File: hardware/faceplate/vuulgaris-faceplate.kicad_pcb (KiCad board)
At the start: 4 copper layers, 298.3 x 137.8 mm, 54 parts, among them J1 HX JN2.54-2x5P TP H8.9, U1 MSP430FR2675TPT, Y1 32.768kHz FC-135 12.5pF

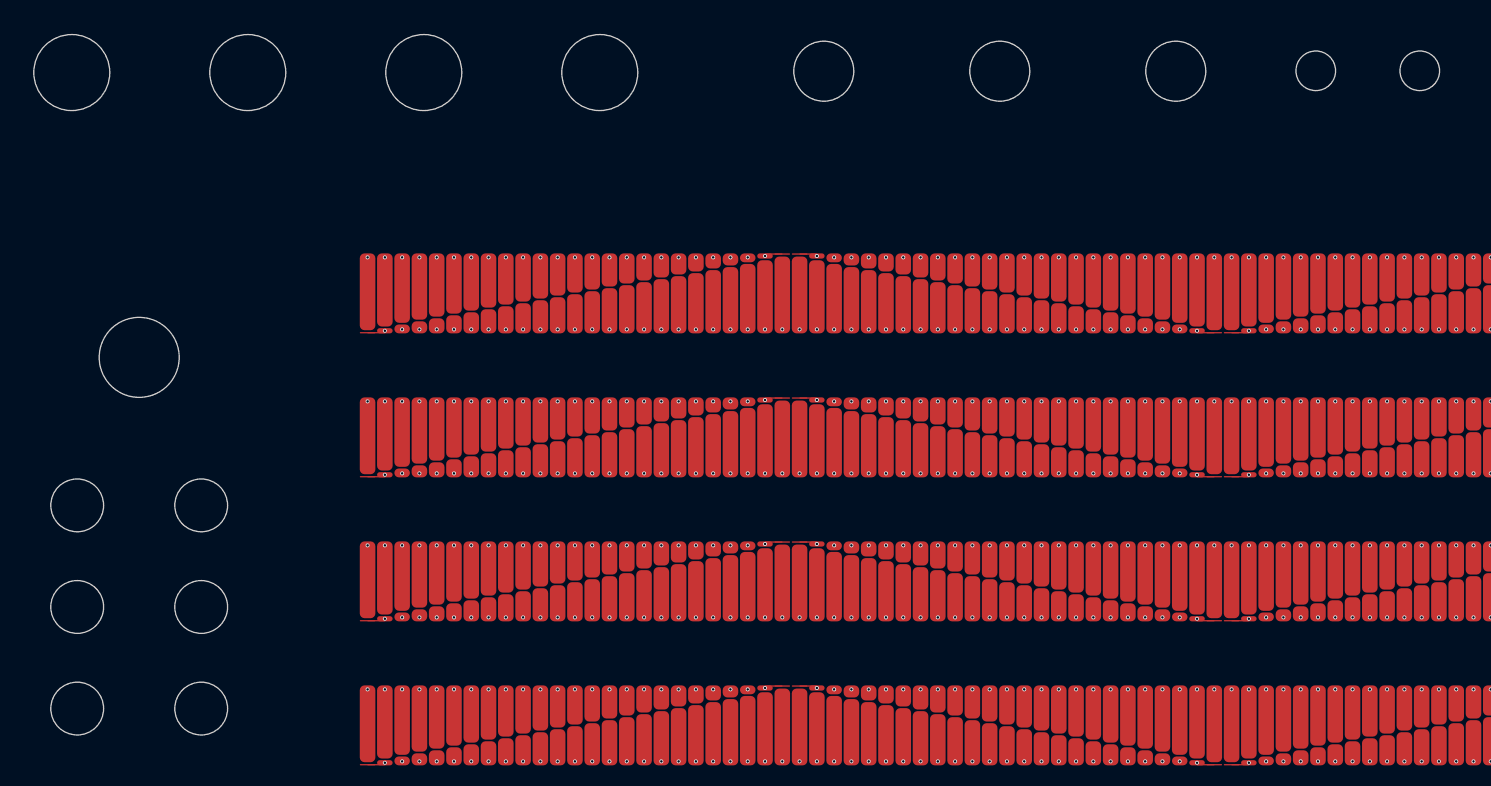
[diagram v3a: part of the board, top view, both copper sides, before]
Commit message: faceplate: bigger button and toggle holes; OLED pixels and glass on F.Fab
Dylan: the button and switch holes look too tight. They were, both by
the drawings:

- Buttons 6.6 -> 7.2. TS1103S: the plunger is 6.2 at our 14mm height and
  one-decimal dimensions are +-0.2, so a 6.4 plunger had 0.1 a side --
  under the faceplate's own +-0.25 float on the pots. A plunger that
  touches its hole is a sticky button. Now 0.4 a side at the largest.
  The generator's mx_hole_r_mm feeds the control-column layout (a bigger
  value re-flows SW4-SW9 on the routed main board -- tried), so it stays
  as the layout value and the new mx_cut_d_mm is what gets routed; the
  physical checks (walls, pads, plunger) use the cut, placement file
  unchanged.
- Toggles 4.95 -> 5.6. Dailywell's bushing is 10-48 UNS, 4.83 over the
  thread; its 4.95 is the hole for a switch hung from the panel by its
  nut. Ours is soldered to the main board too, so the hole takes the
  bushing's +-0.25 and the faceplate's float: 0.39 a side.

New generator rows check both clearances; at the old sizes they fail
(0.10 and 0.06 a side). design-state and the README hole table updated.

Also, as asked: the OLED's active area and glass drawn on the faceplate's
F.Fab from the same numbers as the window (reference only, not
fabricated), so the window reads against the pixels in Pcbnew. mkholes
collects before removing (KiCad 7 bindings again) and is idempotent.

Checked: generator --check all pass, placement unchanged; mksch/netcheck
145/145; boardcheck parity 0, clearance 0; DRC --unrouted 0 errors;
panelcheck --strict 13 OK, 23 holes on their parts; place.py all 24.
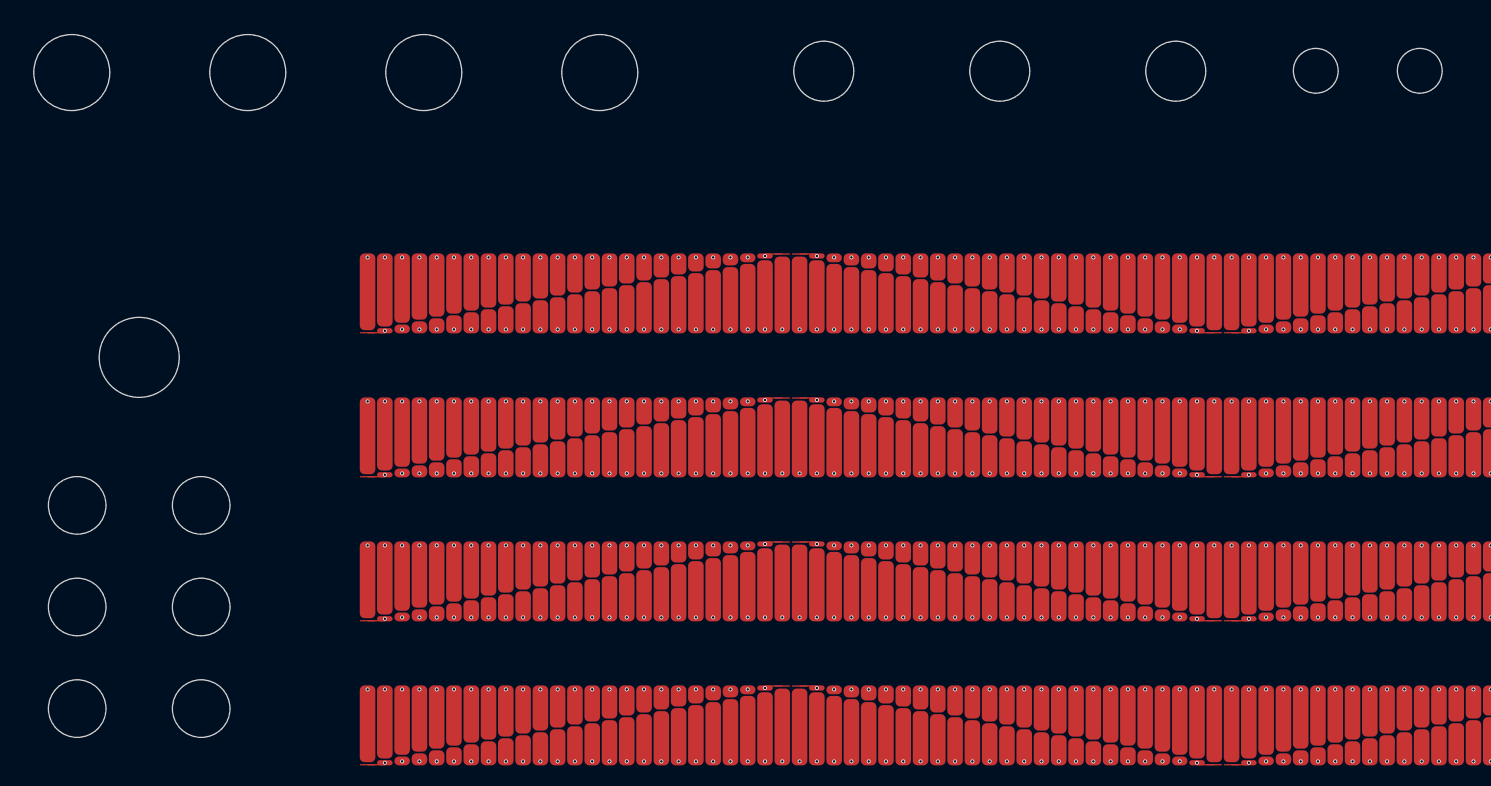
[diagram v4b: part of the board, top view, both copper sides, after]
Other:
- outline, holes or cut-outs redrawn
- board text added: "OLED glass 62.10 x 39.85 -- black past the pixels"
- board text added: "OLED pixels (active area) 55.01 x 27.49"
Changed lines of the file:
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@@
     )
   )
-  (gr_circle (center 125.821 169.353) (end 129.121 169.353)
+  (gr_circle (center 169.143 73.395) (end 173.893 73.395)
     (stroke (width 0.1) (type default)) (fill none) (layer "Edge.Cuts"))
-  (gr_circle (center 169.143 73.395) (end 173.893 73.395)
+  (gr_circle (center 125.821 169.353) (end 129.420999 169.353)
+    (stroke (width 0.1) (type default)) (fill none) (layer "Edge.Cuts"))
+  (gr_circle (center 241.143 89.681) (end 244.893 89.681)
+    (stroke (width 0.1) (type default)) (fill none) (layer "Edge.Cuts"))
+  (gr_circle (center 219.143 89.681) (end 222.893 89.681)
+    (stroke (width 0.1) (type default)) (fill none) (layer "Edge.Cuts"))
+  (gr_circle (center 293.643 89.631) (end 296.443 89.631)
+    (stroke (width 0.1) (type default)) (fill none) (layer "Edge.Cuts"))
+  (gr_line (start 308.502515 98.048499) (end 308.502515 66.1485)
+    (stroke (width 0.1) (type default)) (layer "Edge.Cuts"))
+  (gr_circle (center 191.143 73.395) (end 195.893 73.395)
+    (stroke (width 0.1) (type default)) (fill none) (layer "Edge.Cuts"))
+  (gr_circle (center 280.643 89.631) (end 283.443 89.631)
+    (stroke (width 0.1) (type default)) (fill none) (layer "Edge.Cuts"))
+  (gr_circle (center 133.571 125.453) (end 138.571 125.453)
+    (stroke (width 0.1) (type default)) (fill none) (layer "Edge.Cuts"))
+  (gr_circle (center 125.143 73.395) (end 129.893 73.395)
+    (stroke (width 0.1) (type default)) (fill none) (layer "Edge.Cuts"))
+  (gr_circle (center 263.143 89.681) (end 266.893 89.681)
+    (stroke (width 0.1) (type default)) (fill none) (layer "Edge.Cuts"))
+  (gr_line (start 309.502515 65.1485) (end 367.592857 65.1485)
+    (stroke (width 0.1) (type default)) (layer "Edge.Cuts"))
+  (gr_circle (center 141.321 169.353) (end 144.921 169.353)
+    (stroke (width 0.1) (type default)) (fill none) (layer "Edge.Cuts"))
+  (gr_circle (center 147.143 73.395) (end 151.893 73.395)
+    (stroke (width 0.1) (type default)) (fill none) (layer "Edge.Cuts"))
+  (gr_rect (start 100 50) (end 398.285714 187.81)
+    (stroke (width 0.1) (type default)) (fill none) (layer "Edge.Cuts"))
+  (gr_circle (center 125.821 156.653) (end 129.420999 156.653)
+    (stroke (width 0.1) (type default)) (fill none) (layer "Edge.Cuts"))
+  (gr_circle (center 241.143 73.225) (end 244.893 73.225)
+    (stroke (width 0.1) (type default)) (fill none) (layer "Edge.Cuts"))
+  (gr_arc (start 309.502515 99.048499) (mid 308.795409 98.755606) (end 308.502515 98.048499)
+    (stroke (width 0.1) (type default)) (layer "Edge.Cuts"))
+  (gr_circle (center 263.143 73.225) (end 266.893 73.225)
     (stroke (width 0.1) (type default)) (fill none) (layer "Edge.Cuts"))
   (gr_arc (start 308.502515 66.1485) (mid 308.795409 65.441393) (end 309.502515 65.1485)
     (stroke (width 0.1) (type default)) (layer "Edge.Cuts"))
-  (gr_circle (center 219.143 89.681) (end 222.893 89.681)
-    (stroke (width 0.1) (type default)) (fill none) (layer "Edge.Cuts"))
-  (gr_circle (center 263.143 89.681) (end 266.893 89.681)
-    (stroke (width 0.1) (type default)) (fill none) (layer "Edge.Cuts"))
-  (gr_line (start 308.502515 98.048499) (end 308.502515 66.1485)
-    (stroke (width 0.1) (type default)) (layer "Edge.Cuts"))
   (gr_circle (center 125.143 89.851) (end 129.893 89.851)
     (stroke (width 0.1) (type default)) (fill none) (layer "Edge.Cuts"))
-  (gr_circle (center 147.143 73.395) (end 151.893 73.395)
-    (stroke (width 0.1) (type default)) (fill none) (layer "Edge.Cuts"))
-  (gr_circle (center 191.143 73.395) (end 195.893 73.395)
-    (stroke (width 0.1) (type default)) (fill none) (layer "Edge.Cuts"))
-  (gr_circle (center 141.321 143.953) (end 144.621 143.953)
-    (stroke (width 0.1) (type default)) (fill none) (layer "Edge.Cuts"))
-  (gr_circle (center 125.821 143.953) (end 129.121 143.953)
-    (stroke (width 0.1) (type default)) (fill none) (layer "Edge.Cuts"))
-  (gr_arc (start 309.502515 99.048499) (mid 308.795409 98.755606) (end 308.502515 98.048499)
+  (gr_line (start 367.592857 99.048499) (end 309.502515 99.048499)
     (stroke (width 0.1) (type default)) (layer "Edge.Cuts"))
-  (gr_rect (start 100 50) (end 398.285714 187.81)
-    (stroke (width 0.1) (type default)) (fill none) (layer "Edge.Cuts"))
-  (gr_circle (center 125.143 73.395) (end 129.893 73.395)
-    (stroke (width 0.1) (type default)) (fill none) (layer "Edge.Cuts"))
-  (gr_arc (start 367.592857 65.1485) (mid 368.299963 65.441393) (end 368.592857 66.1485)
-    (stroke (width 0.1) (type default)) (layer "Edge.Cuts"))
-  (gr_circle (center 191.143 89.851) (end 195.893 89.851)
-    (stroke (width 0.1) (type default)) (fill none) (layer "Edge.Cuts"))
-  (gr_circle (center 241.143 89.681) (end 244.893 89.681)
+  (gr_circle (center 219.143 73.225) (end 222.893 73.225)
     (stroke (width 0.1) (type default)) (fill none) (layer "Edge.Cuts"))
   (gr_arc (start 368.592857 98.048499) (mid 368.299963 98.755606) (end 367.592857 99.048499)
     (stroke (width 0.1) (type default)) (layer "Edge.Cuts"))
-  (gr_circle (center 293.643 89.631) (end 296.118 89.631)
+  (gr_circle (center 141.321 156.653) (end 144.921 156.653)
     (stroke (width 0.1) (type default)) (fill none) (layer "Edge.Cuts"))
-  (gr_circle (center 241.143 73.225) (end 244.893 73.225)
-    (stroke (width 0.1) (type default)) (fill none) (layer "Edge.Cuts"))
-  (gr_line (start 367.592857 99.048499) (end 309.502515 99.048499)
-    (stroke (width 0.1) (type default)) (layer "Edge.Cuts"))
   (gr_line (start 368.592857 66.1485) (end 368.592857 98.048499)
     (stroke (width 0.1) (type default)) (layer "Edge.Cuts"))
-  (gr_circle (center 141.321 156.653) (end 144.621 156.653)
-    (stroke (width 0.1) (type default)) (fill none) (layer "Edge.Cuts"))
-  (gr_circle (center 125.821 156.653) (end 129.121 156.653)
+  (gr_arc (start 367.592857 65.1485) (mid 368.299963 65.441393) (end 368.592857 66.1485)
+    (stroke (width 0.1) (type default)) (layer "Edge.Cuts"))
+  (gr_circle (center 125.821 143.953) (end 129.420999 143.953)
     (stroke (width 0.1) (type default)) (fill none) (layer "Edge.Cuts"))
   (gr_circle (center 169.143 89.851) (end 173.893 89.851)
     (stroke (width 0.1) (type default)) (fill none) (layer "Edge.Cuts"))
-  (gr_circle (center 219.143 73.225) (end 222.893 73.225)
-    (stroke (width 0.1) (type default)) (fill none) (layer "Edge.Cuts"))
-  (gr_circle (center 133.571 125.453) (end 138.571 125.453)
-    (stroke (width 0.1) (type default)) (fill none) (layer "Edge.Cuts"))
   (gr_circle (center 147.143 89.851) (end 151.893 89.851)
     (stroke (width 0.1) (type default)) (fill none) (layer "Edge.Cuts"))
-  (gr_line (start 309.502515 65.1485) (end 367.592857 65.1485)
-    (stroke (width 0.1) (type default)) (layer "Edge.Cuts"))
-  (gr_circle (center 141.321 169.353) (end 144.621 169.353)
+  (gr_circle (center 141.321 143.953) (end 144.921 143.953)
     (stroke (width 0.1) (type default)) (fill none) (layer "Edge.Cuts"))
-  (gr_circle (center 280.643 89.631) (end 283.118 89.631)
+  (gr_circle (center 191.143 89.851) (end 195.893 89.851)
     (stroke (width 0.1) (type default)) (fill none) (layer "Edge.Cuts"))
-  (gr_circle (center 263.143 73.225) (end 266.893 73.225)
-    (stroke (width 0.1) (type default)) (fill none) (layer "Edge.Cuts"))
+  (gr_rect (start 307.492857 64.1485) (end 369.592857 103.9985)
+    (stroke (width 0.1) (type default)) (fill none) (layer "F.Fab"))
+  (gr_rect (start 311.042857 67.1585) (end 366.052857 94.6485)
+    (stroke (width 0.1) (type default)) (fill none) (layer "F.Fab"))
+  (gr_text "OLED pixels (active area) 55.01 x 27.49" (at 312.042857 68.5585) (layer "F.Fab")
+    (effects (font (size 1 1) (thickness 0.15)) (justify left))
+  )
+  (gr_text "OLED glass 62.10 x 39.85 -- black past the pixels" (at 308.492857 102.5985) (layer "F.Fab")
+    (effects (font (size 1 1) (thickness 0.15)) (justify left))
+  )
   (segment (start 331.535 159.075) (end 334.075 159.075) (width 0.5) (layer "B.Cu") (net 1))
   (segment (start 328.995 159.075) (end 331.535 159.075) (width 0.5) (layer "B.Cu") (net 1))
